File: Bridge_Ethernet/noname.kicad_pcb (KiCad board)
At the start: 2 copper layers, 67 x 85 mm, 86 parts, among them J1 Conn_01x04_Female, J2 Conn_01x04_Female, J3 Conn_01x06, J4 Conn_01x06, J5 Conn_2Rows-13Pins, J7 Conn_01x04_Male, U1 MAX3222CDW, U10 MAX3222CDW, U11 ISL83485, U12 MAX3222CDW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

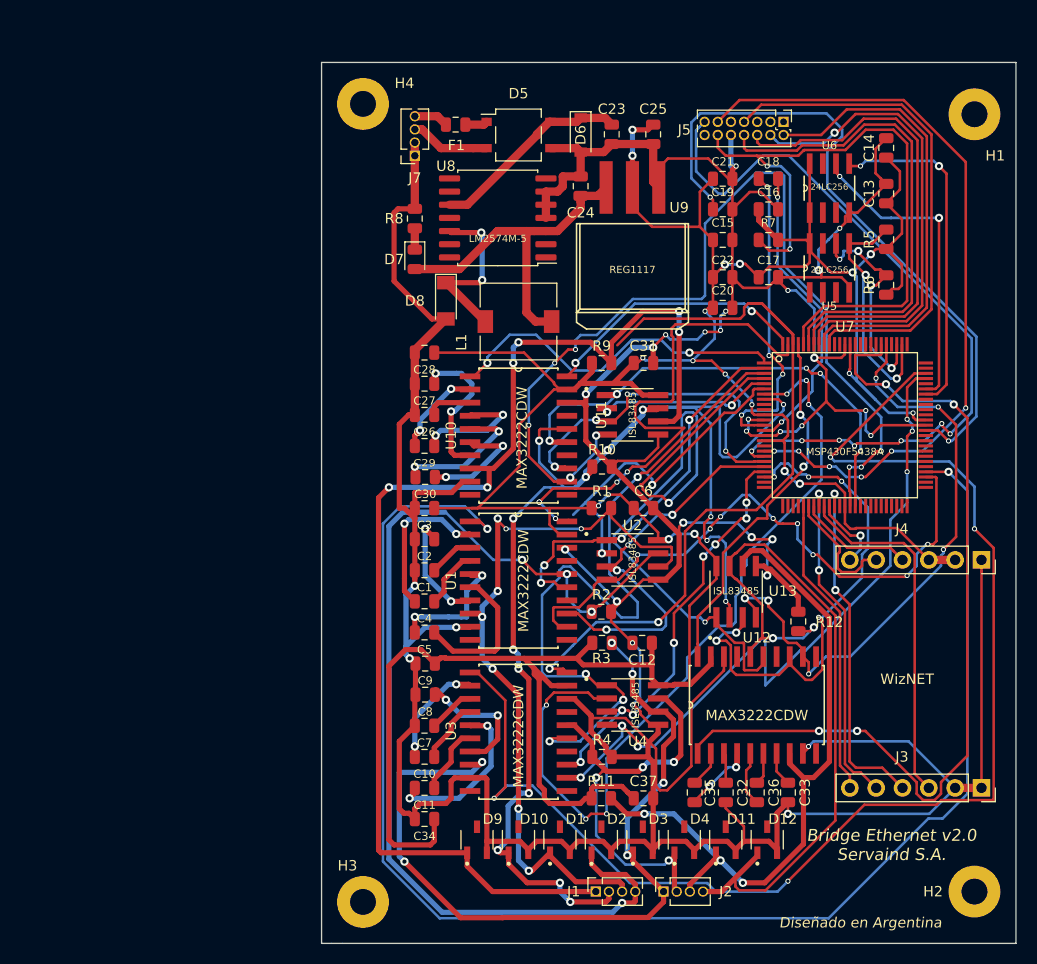
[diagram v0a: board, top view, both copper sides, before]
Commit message: v2.0. Faltan algunos componentes 3D. Correciones relizadas.
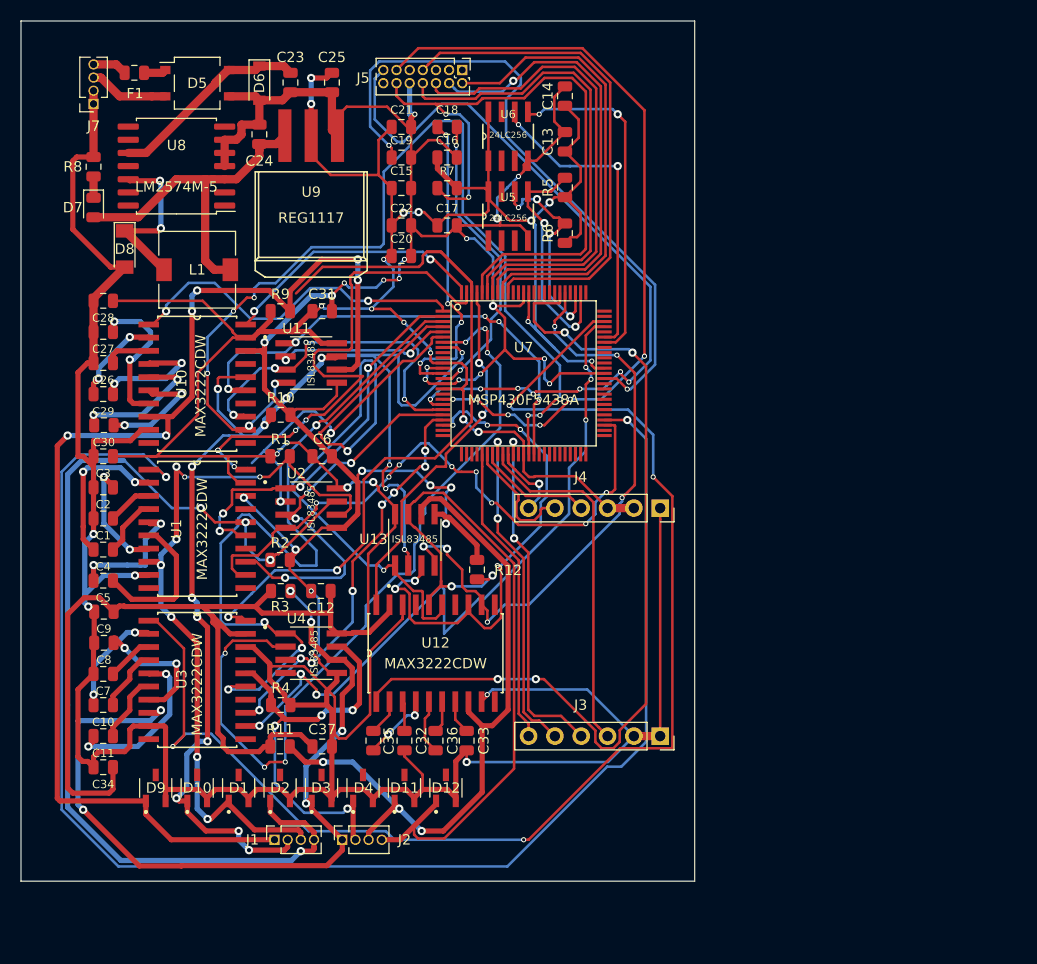
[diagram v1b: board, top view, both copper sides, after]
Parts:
- removed H1, H2, H3, H4: MountingHole, MountingHole:MountingHole_2.5mm_Pad
- moved C16 31.4 mm to (59.1, 86.2)
- moved C17 31.4 mm to (59.1, 92.7)
- moved C18 31.4 mm to (59.1, 83.2)
- moved R7 31.4 mm to (59.1, 89.1)
- moved C1 31.4 mm to (25.9, 121.0)
- moved C10 31.4 mm to (25.9, 139.0)
- moved C11 31.4 mm to (25.9, 142.0)
- moved C12 31.4 mm to (46.9, 128.0)
- moved C13 31.4 mm to (70.5, 84.7)
- moved C14 31.4 mm to (70.5, 80.2)
- moved C2 31.4 mm to (25.9, 118.0)
- moved C23 31.4 mm to (44.0, 78.9)
- moved C24 31.4 mm to (41.0, 83.9)
- moved C25 31.4 mm to (48.0, 78.9)
- moved C26 31.4 mm to (25.9, 106.0)
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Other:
- board size 67 x 85 mm -> 65 x 83 mm
- board text removed: "Bridge Ethernet v2.0 Servaind S.A."
- board text removed: "Diseñado en Argentina"
- board text removed: "Grillas: 1 mm/0,5 mm/0,25mm Ancho de Pistas: 0,8 mm/0,5 mm/0,25 mm Ancho de vía/agujero de vía: 0,8/0,4 mm y 0,5/0,3 mm Fabricante de Referencia: Mayer Dimensiones en Capa Dwgs.User"
- board text removed: "WizNET"
